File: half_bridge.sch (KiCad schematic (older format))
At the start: 9 parts, among them Q11 MOSFET_N, Q12 MOSFET_N, U6 IR2184

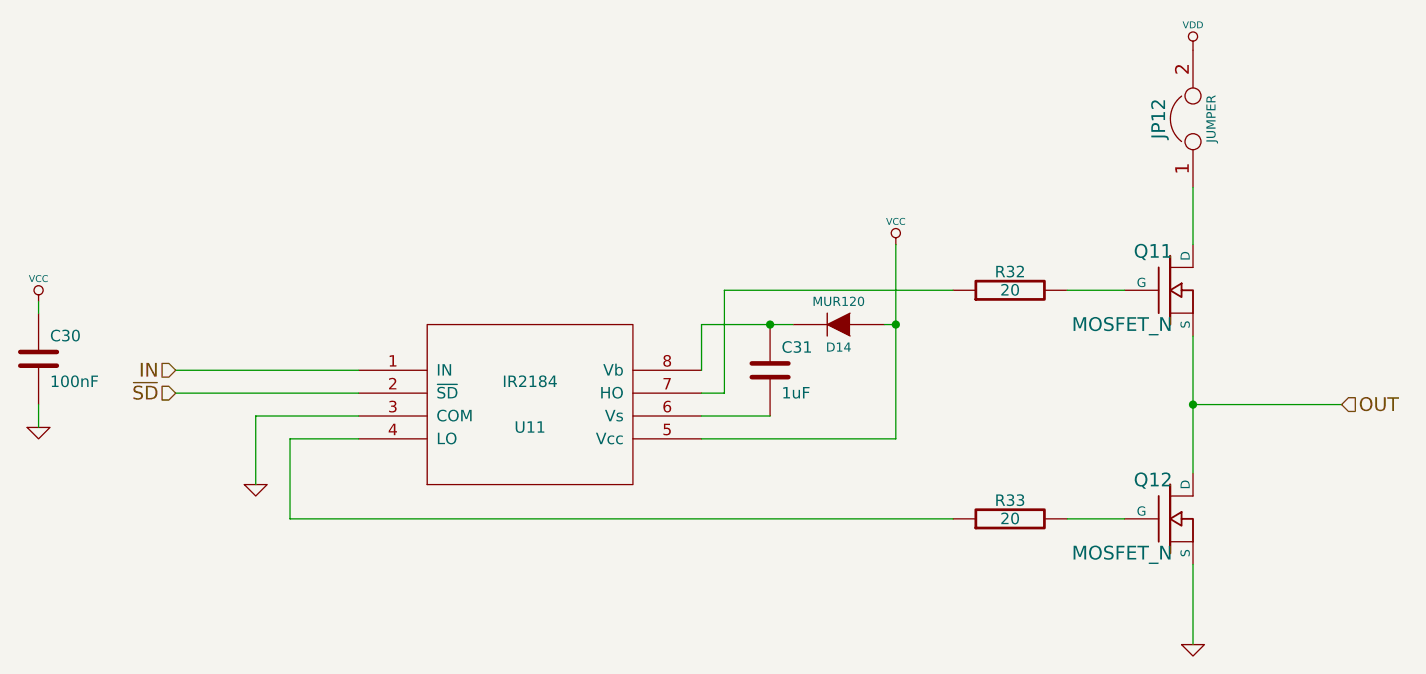
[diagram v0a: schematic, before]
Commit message: Change IR2184 to Vdd instead of Vcc
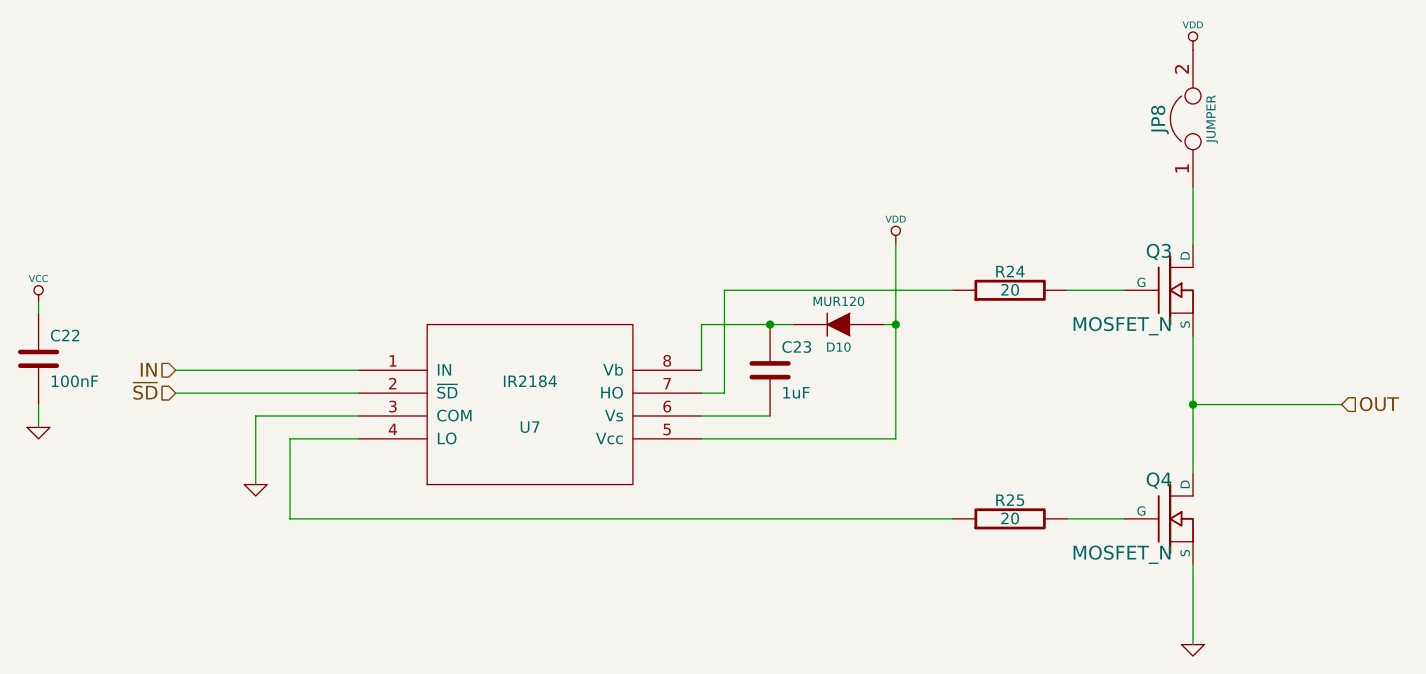
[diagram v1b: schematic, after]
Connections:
- net VCC: no longer D14.1 (A), U6.5 (Vcc)
- net VDD: now also D14.1 (A), U6.5 (Vcc)
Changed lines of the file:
@@
-EESchema Schematic File Version 2  date Fri 27 Dec 2013 06:54:03 PM EST
+EESchema Schematic File Version 2  date Sat 28 Dec 2013 06:57:52 PM EST
 LIBS:power
 LIBS:device
@@
 $Descr A4 11700 8267
 encoding utf-8
-Sheet 7 7
+Sheet 3 7
 Title "noname.sch"
-Date "27 dec 2013"
+Date "28 dec 2013"
 Rev ""
 Comp ""
@@
 Comment4 ""
 $EndDescr
+$Comp
+L VDD #PWR?
+U 1 1 52BF650C
+P 6250 2150
+F 0 "#PWR?" H 6250 2250 30  0001 C CNN
+F 1 "VDD" H 6250 2260 30  0000 C CNN
+	1    6250 2150
+	1    0    0    -1
+$EndComp
 Wire Wire Line
 	2500 2400 2500 2450
@@
 	2500 2850 2500 2950
 $Comp
-L GND #PWR066
+L GND #PWR070
 U 1 1 527843FF
 P 2500 2950
-AR Path="/52783E14/527843FF" Ref="#PWR066"  Part="1"
-AR Path="/52783E7D/527843FF" Ref="#PWR072"  Part="1"
-AR Path="/52783E4E/527843FF" Ref="#PWR078"  Part="1"
-AR Path="/52783E34/527843FF" Ref="#PWR084"  Part="1"
-AR Path="/52783943/527843FF" Ref="#PWR090"  Part="1"
-AR Path="/5278392A/527843FF" Ref="#PWR096"  Part="1"
-F 0 "#PWR096" H 2500 2950 30  0001 C CNN
+AR Path="/52783E14/527843FF" Ref="#PWR070"  Part="1"
+AR Path="/52783E7D/527843FF" Ref="#PWR076"  Part="1"
+AR Path="/52783E4E/527843FF" Ref="#PWR082"  Part="1"
+AR Path="/52783E34/527843FF" Ref="#PWR088"  Part="1"
+AR Path="/52783943/527843FF" Ref="#PWR094"  Part="1"
+AR Path="/5278392A/527843FF" Ref="#PWR0100"  Part="1"
+F 0 "#PWR076" H 2500 2950 30  0001 C CNN
 F 1 "GND" H 2500 2880 30  0001 C CNN
 	1    2500 2950
@@
 AR Path="/52783943/527843E9" Ref="C28"  Part="1"
 AR Path="/5278392A/527843E9" Ref="C30"  Part="1"
-F 0 "C30" H 2550 2750 50  0000 L CNN
+F 0 "C22" H 2550 2750 50  0000 L CNN
 F 1 "100nF" H 2550 2550 50  0000 L CNN
 	1    2500 2650
@@
 $EndComp
 $Comp
-L VCC #PWR067
+L VCC #PWR071
 U 1 1 527843E4
 P 2500 2400
-AR Path="/52783E14/527843E4" Ref="#PWR067"  Part="1"
-AR Path="/52783E7D/527843E4" Ref="#PWR073"  Part="1"
-AR Path="/52783E4E/527843E4" Ref="#PWR079"  Part="1"
-AR Path="/52783E34/527843E4" Ref="#PWR085"  Part="1"
-AR Path="/52783943/527843E4" Ref="#PWR091"  Part="1"
-AR Path="/5278392A/527843E4" Ref="#PWR097"  Part="1"
-F 0 "#PWR097" H 2500 2500 30  0001 C CNN
+AR Path="/52783E14/527843E4" Ref="#PWR071"  Part="1"
+AR Path="/52783E7D/527843E4" Ref="#PWR077"  Part="1"
+AR Path="/52783E4E/527843E4" Ref="#PWR083"  Part="1"
+AR Path="/52783E34/527843E4" Ref="#PWR089"  Part="1"
+AR Path="/52783943/527843E4" Ref="#PWR095"  Part="1"
+AR Path="/5278392A/527843E4" Ref="#PWR0101"  Part="1"
+F 0 "#PWR077" H 2500 2500 30  0001 C CNN
 F 1 "VCC" H 2500 2500 30  0000 C CNN
 	1    2500 2400
@@
 AR Path="/52783E34/527838B2" Ref="R29"  Part="1"
 AR Path="/52783943/527838B2" Ref="R31"  Part="1"
-F 0 "R33" V 6830 3350 50  0000 C CNN
+F 0 "R25" V 6830 3350 50  0000 C CNN
 F 1 "20" V 6750 3350 50  0000 C CNN
 	1    6750 3350
@@
 AR Path="/52783E34/5278387F" Ref="R28"  Part="1"
 AR Path="/52783943/5278387F" Ref="R30"  Part="1"
-F 0 "R32" V 6830 2350 50  0000 C CNN
+F 0 "R24" V 6830 2350 50  0000 C CNN
 F 1 "20" V 6750 2350 50  0000 C CNN
 	1    6750 2350
@@
 AR Path="/52783943/5278382D" Ref="U10"  Part="1"
 AR Path="/5278392A/5278382D" Ref="U11"  Part="1"
-F 0 "U11" H 4650 2750 50  0000 C CNN
+F 0 "U7" H 4650 2750 50  0000 C CNN
 F 1 "IR2184" H 4650 2950 50  0000 C CNN
 F 2 "MODULE" H 4650 2850 50  0001 C CNN
@@
 IN
 $Comp
-L GND #PWR098
+L GND #PWR0102
 U 1 1 52783639
 P 3450 3200
-AR Path="/5278392A/52783639" Ref="#PWR098"  Part="1"
-AR Path="/52783E14/52783639" Ref="#PWR068"  Part="1"
-AR Path="/52783E7D/52783639" Ref="#PWR074"  Part="1"
-AR Path="/52783E4E/52783639" Ref="#PWR080"  Part="1"
-AR Path="/52783E34/52783639" Ref="#PWR086"  Part="1"
-AR Path="/52783943/52783639" Ref="#PWR092"  Part="1"
-F 0 "#PWR098" H 3450 3200 30  0001 C CNN
+AR Path="/5278392A/52783639" Ref="#PWR0102"  Part="1"
+AR Path="/52783E14/52783639" Ref="#PWR072"  Part="1"
+AR Path="/52783E7D/52783639" Ref="#PWR078"  Part="1"
+AR Path="/52783E4E/52783639" Ref="#PWR084"  Part="1"
+AR Path="/52783E34/52783639" Ref="#PWR090"  Part="1"
+AR Path="/52783943/52783639" Ref="#PWR096"  Part="1"
+F 0 "#PWR078" H 3450 3200 30  0001 C CNN
 F 1 "GND" H 3450 3130 30  0001 C CNN
 	1    3450 3200
-	1    0    0    -1
-$EndComp
-$Comp
-L VCC #PWR099
-U 1 1 527835CC
-P 6250 2150
-AR Path="/5278392A/527835CC" Ref="#PWR099"  Part="1"
-AR Path="/52783E14/527835CC" Ref="#PWR069"  Part="1"
-AR Path="/52783E7D/527835CC" Ref="#PWR075"  Part="1"
-AR Path="/52783E4E/527835CC" Ref="#PWR081"  Part="1"
-AR Path="/52783E34/527835CC" Ref="#PWR087"  Part="1"
-AR Path="/52783943/527835CC" Ref="#PWR093"  Part="1"
-F 0 "#PWR099" H 6250 2250 30  0001 C CNN
-F 1 "VCC" H 6250 2250 30  0000 C CNN
-	1    6250 2150
 	1    0    0    -1
 $EndComp
@@
 AR Path="/52783E34/527835B9" Ref="C27"  Part="1"
 AR Path="/52783943/527835B9" Ref="C29"  Part="1"
-F 0 "C31" H 5750 2800 50  0000 L CNN
+F 0 "C23" H 5750 2800 50  0000 L CNN
 F 1 "1uF" H 5750 2600 50  0000 L CNN
 	1    5700 2700
@@
 AR Path="/52783E34/5278358E" Ref="D12"  Part="1"
 AR Path="/52783943/5278358E" Ref="D13"  Part="1"
-F 0 "D14" H 6000 2600 40  0000 C CNN
+F 0 "D10" H 6000 2600 40  0000 C CNN
 F 1 "MUR120" H 6000 2400 40  0000 C CNN
 	1    6000 2500
@@
 AR Path="/52783E34/52783118" Ref="JP10"  Part="1"
 AR Path="/52783943/52783118" Ref="JP11"  Part="1"
-F 0 "JP12" H 7550 1750 60  0000 C CNN
+F 0 "JP8" H 7550 1750 60  0000 C CNN
 F 1 "JUMPER" H 7550 1520 40  0000 C CNN
 	1    7550 1600
@@
 $EndComp
 $Comp
-L GND #PWR0100
+L GND #PWR0104
 U 1 1 52783104
 P 7550 3900
-AR Path="/5278392A/52783104" Ref="#PWR0100"  Part="1"
-AR Path="/52783E14/52783104" Ref="#PWR070"  Part="1"
-AR Path="/52783E7D/52783104" Ref="#PWR076"  Part="1"
-AR Path="/52783E4E/52783104" Ref="#PWR082"  Part="1"
-AR Path="/52783E34/52783104" Ref="#PWR088"  Part="1"
-AR Path="/52783943/52783104" Ref="#PWR094"  Part="1"
-F 0 "#PWR0100" H 7550 3900 30  0001 C CNN
+AR Path="/5278392A/52783104" Ref="#PWR0104"  Part="1"
+AR Path="/52783E14/52783104" Ref="#PWR074"  Part="1"
+AR Path="/52783E7D/52783104" Ref="#PWR080"  Part="1"
+AR Path="/52783E4E/52783104" Ref="#PWR086"  Part="1"
+AR Path="/52783E34/52783104" Ref="#PWR092"  Part="1"
+AR Path="/52783943/52783104" Ref="#PWR098"  Part="1"
+F 0 "#PWR080" H 7550 3900 30  0001 C CNN
 F 1 "GND" H 7550 3830 30  0001 C CNN
 	1    7550 3900
@@
 $EndComp
 $Comp
-L VDD #PWR0101
+L VDD #PWR0105
 U 1 1 527830FD
 P 7550 1300
-AR Path="/5278392A/527830FD" Ref="#PWR0101"  Part="1"
-AR Path="/52783E14/527830FD" Ref="#PWR071"  Part="1"
-AR Path="/52783E7D/527830FD" Ref="#PWR077"  Part="1"
-AR Path="/52783E4E/527830FD" Ref="#PWR083"  Part="1"
-AR Path="/52783E34/527830FD" Ref="#PWR089"  Part="1"
-AR Path="/52783943/527830FD" Ref="#PWR095"  Part="1"
-F 0 "#PWR0101" H 7550 1400 30  0001 C CNN
+AR Path="/5278392A/527830FD" Ref="#PWR0105"  Part="1"
+AR Path="/52783E14/527830FD" Ref="#PWR075"  Part="1"
+AR Path="/52783E7D/527830FD" Ref="#PWR081"  Part="1"
+AR Path="/52783E4E/527830FD" Ref="#PWR087"  Part="1"
+AR Path="/52783E34/527830FD" Ref="#PWR093"  Part="1"
+AR Path="/52783943/527830FD" Ref="#PWR099"  Part="1"
+F 0 "#PWR081" H 7550 1400 30  0001 C CNN
 F 1 "VDD" H 7550 1410 30  0000 C CNN
 	1    7550 1300
@@
 AR Path="/52783E34/527830EC" Ref="Q8"  Part="1"
 AR Path="/52783943/527830EC" Ref="Q10"  Part="1"
-F 0 "Q12" H 7460 3520 60  0000 R CNN
+F 0 "Q4" H 7460 3520 60  0000 R CNN
 F 1 "MOSFET_N" H 7460 3200 60  0000 R CNN
 	1    7450 3350
@@
 AR Path="/52783E34/527830DE" Ref="Q7"  Part="1"
 AR Path="/52783943/527830DE" Ref="Q9"  Part="1"
-F 0 "Q11" H 7460 2520 60  0000 R CNN
+F 0 "Q3" H 7460 2520 60  0000 R CNN
 F 1 "MOSFET_N" H 7460 2200 60  0000 R CNN
 	1    7450 2350

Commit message: Added second power connector
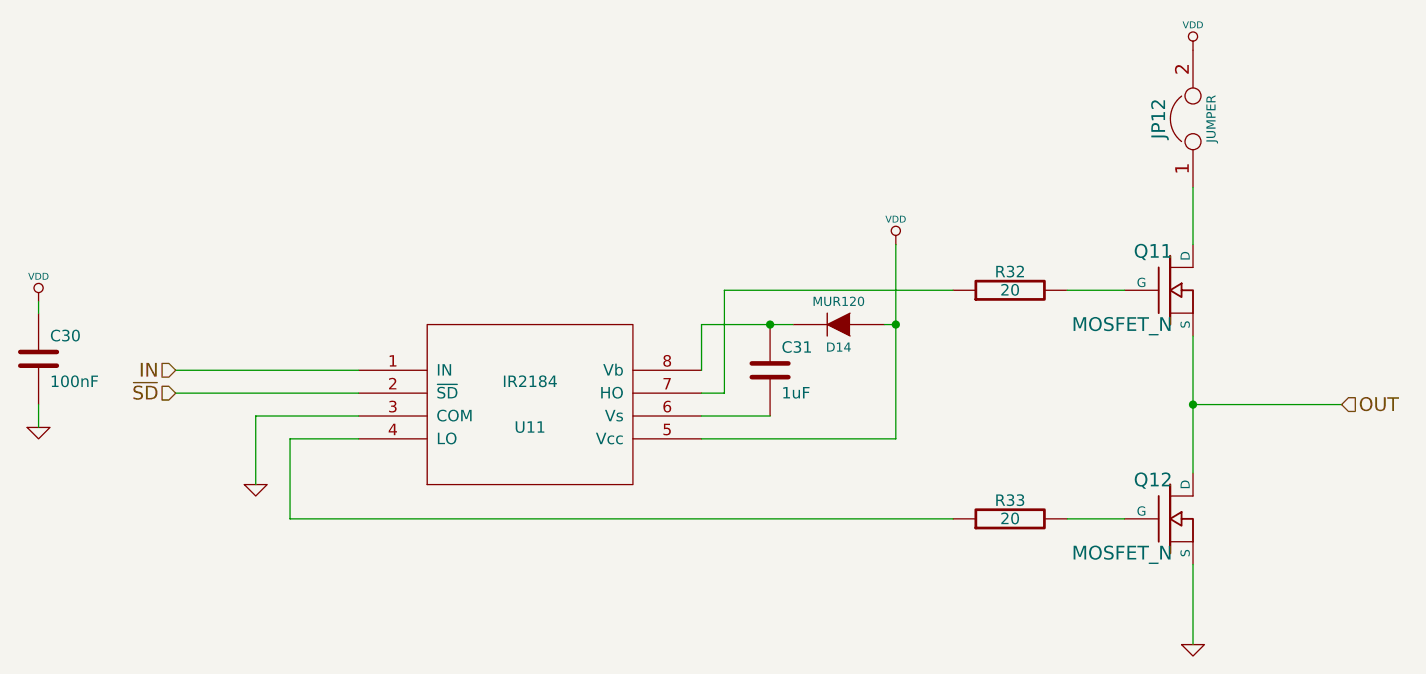
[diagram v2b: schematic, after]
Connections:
- net VCC is gone; now on net VDD: C20.1
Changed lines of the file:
@@
-EESchema Schematic File Version 2  date Sat 28 Dec 2013 06:57:52 PM EST
+EESchema Schematic File Version 2  date Thu 02 Jan 2014 06:39:32 PM EST
 LIBS:power
 LIBS:device
@@
 LIBS:-cache
 LIBS:LM25011
+LIBS:open-project
 LIBS:hackboard-cache
 EELAYER 25  0
@@
 $Descr A4 11700 8267
 encoding utf-8
-Sheet 3 7
+Sheet 4 7
 Title "noname.sch"
-Date "28 dec 2013"
+Date "2 jan 2014"
 Rev ""
 Comp ""
@@
 $EndDescr
 $Comp
-L VDD #PWR?
+L VDD #PWR70
+U 1 1 52BF660C
+P 2500 2400
+AR Path="/52783E14/52BF660C" Ref="#PWR70"  Part="1"
+AR Path="/52783E7D/52BF660C" Ref="#PWR76"  Part="1"
+AR Path="/52783E4E/52BF660C" Ref="#PWR82"  Part="1"
+AR Path="/52783E34/52BF660C" Ref="#PWR88"  Part="1"
+AR Path="/52783943/52BF660C" Ref="#PWR94"  Part="1"
+AR Path="/5278392A/52BF660C" Ref="#PWR100"  Part="1"
+F 0 "#PWR100" H 2500 2500 30  0001 C CNN
+F 1 "VDD" H 2500 2510 30  0000 C CNN
+	1    2500 2400
+	1    0    0    -1
+$EndComp
+$Comp
+L VDD #PWR79
 U 1 1 52BF650C
 P 6250 2150
-F 0 "#PWR?" H 6250 2250 30  0001 C CNN
+AR Path="/52783E7D/52BF650C" Ref="#PWR79"  Part="1"
+AR Path="/52783E14/52BF650C" Ref="#PWR73"  Part="1"
+AR Path="/52783E4E/52BF650C" Ref="#PWR85"  Part="1"
+AR Path="/52783E34/52BF650C" Ref="#PWR91"  Part="1"
+AR Path="/52783943/52BF650C" Ref="#PWR97"  Part="1"
+AR Path="/5278392A/52BF650C" Ref="#PWR103"  Part="1"
+F 0 "#PWR103" H 6250 2250 30  0001 C CNN
 F 1 "VDD" H 6250 2260 30  0000 C CNN
 	1    6250 2150
@@
 	2500 2850 2500 2950
 $Comp
-L GND #PWR070
+L GND #PWR71
 U 1 1 527843FF
 P 2500 2950
-AR Path="/52783E14/527843FF" Ref="#PWR070"  Part="1"
-AR Path="/52783E7D/527843FF" Ref="#PWR076"  Part="1"
-AR Path="/52783E4E/527843FF" Ref="#PWR082"  Part="1"
-AR Path="/52783E34/527843FF" Ref="#PWR088"  Part="1"
-AR Path="/52783943/527843FF" Ref="#PWR094"  Part="1"
-AR Path="/5278392A/527843FF" Ref="#PWR0100"  Part="1"
-F 0 "#PWR076" H 2500 2950 30  0001 C CNN
+AR Path="/52783E14/527843FF" Ref="#PWR71"  Part="1"
+AR Path="/52783E7D/527843FF" Ref="#PWR77"  Part="1"
+AR Path="/52783E4E/527843FF" Ref="#PWR83"  Part="1"
+AR Path="/52783E34/527843FF" Ref="#PWR89"  Part="1"
+AR Path="/52783943/527843FF" Ref="#PWR95"  Part="1"
+AR Path="/5278392A/527843FF" Ref="#PWR101"  Part="1"
+F 0 "#PWR101" H 2500 2950 30  0001 C CNN
 F 1 "GND" H 2500 2880 30  0001 C CNN
 	1    2500 2950
@@
 AR Path="/52783943/527843E9" Ref="C28"  Part="1"
 AR Path="/5278392A/527843E9" Ref="C30"  Part="1"
-F 0 "C22" H 2550 2750 50  0000 L CNN
+F 0 "C30" H 2550 2750 50  0000 L CNN
 F 1 "100nF" H 2550 2550 50  0000 L CNN
 	1    2500 2650
-	1    0    0    -1
-$EndComp
-$Comp
-L VCC #PWR071
-U 1 1 527843E4
-P 2500 2400
-AR Path="/52783E14/527843E4" Ref="#PWR071"  Part="1"
-AR Path="/52783E7D/527843E4" Ref="#PWR077"  Part="1"
-AR Path="/52783E4E/527843E4" Ref="#PWR083"  Part="1"
-AR Path="/52783E34/527843E4" Ref="#PWR089"  Part="1"
-AR Path="/52783943/527843E4" Ref="#PWR095"  Part="1"
-AR Path="/5278392A/527843E4" Ref="#PWR0101"  Part="1"
-F 0 "#PWR077" H 2500 2500 30  0001 C CNN
-F 1 "VCC" H 2500 2500 30  0000 C CNN
-	1    2500 2400
 	1    0    0    -1
 $EndComp
@@
 AR Path="/52783E34/527838B2" Ref="R29"  Part="1"
 AR Path="/52783943/527838B2" Ref="R31"  Part="1"
-F 0 "R25" V 6830 3350 50  0000 C CNN
+F 0 "R33" V 6830 3350 50  0000 C CNN
 F 1 "20" V 6750 3350 50  0000 C CNN
 	1    6750 3350
@@
 AR Path="/52783E34/5278387F" Ref="R28"  Part="1"
 AR Path="/52783943/5278387F" Ref="R30"  Part="1"
-F 0 "R24" V 6830 2350 50  0000 C CNN
+F 0 "R32" V 6830 2350 50  0000 C CNN
 F 1 "20" V 6750 2350 50  0000 C CNN
 	1    6750 2350
@@
 AR Path="/52783943/5278382D" Ref="U10"  Part="1"
 AR Path="/5278392A/5278382D" Ref="U11"  Part="1"
-F 0 "U7" H 4650 2750 50  0000 C CNN
+F 0 "U11" H 4650 2750 50  0000 C CNN
 F 1 "IR2184" H 4650 2950 50  0000 C CNN
 F 2 "MODULE" H 4650 2850 50  0001 C CNN
@@
 IN
 $Comp
-L GND #PWR0102
+L GND #PWR102
 U 1 1 52783639
 P 3450 3200
-AR Path="/5278392A/52783639" Ref="#PWR0102"  Part="1"
-AR Path="/52783E14/52783639" Ref="#PWR072"  Part="1"
-AR Path="/52783E7D/52783639" Ref="#PWR078"  Part="1"
-AR Path="/52783E4E/52783639" Ref="#PWR084"  Part="1"
-AR Path="/52783E34/52783639" Ref="#PWR090"  Part="1"
-AR Path="/52783943/52783639" Ref="#PWR096"  Part="1"
-F 0 "#PWR078" H 3450 3200 30  0001 C CNN
+AR Path="/5278392A/52783639" Ref="#PWR102"  Part="1"
+AR Path="/52783E14/52783639" Ref="#PWR72"  Part="1"
+AR Path="/52783E7D/52783639" Ref="#PWR78"  Part="1"
+AR Path="/52783E4E/52783639" Ref="#PWR84"  Part="1"
+AR Path="/52783E34/52783639" Ref="#PWR90"  Part="1"
+AR Path="/52783943/52783639" Ref="#PWR96"  Part="1"
+F 0 "#PWR102" H 3450 3200 30  0001 C CNN
 F 1 "GND" H 3450 3130 30  0001 C CNN
 	1    3450 3200
@@
 AR Path="/52783E34/527835B9" Ref="C27"  Part="1"
 AR Path="/52783943/527835B9" Ref="C29"  Part="1"
-F 0 "C23" H 5750 2800 50  0000 L CNN
+F 0 "C31" H 5750 2800 50  0000 L CNN
 F 1 "1uF" H 5750 2600 50  0000 L CNN
 	1    5700 2700
@@
 AR Path="/52783E34/5278358E" Ref="D12"  Part="1"
 AR Path="/52783943/5278358E" Ref="D13"  Part="1"
-F 0 "D10" H 6000 2600 40  0000 C CNN
+F 0 "D14" H 6000 2600 40  0000 C CNN
 F 1 "MUR120" H 6000 2400 40  0000 C CNN
 	1    6000 2500
@@
 AR Path="/52783E34/52783118" Ref="JP10"  Part="1"
 AR Path="/52783943/52783118" Ref="JP11"  Part="1"
-F 0 "JP8" H 7550 1750 60  0000 C CNN
+F 0 "JP12" H 7550 1750 60  0000 C CNN
 F 1 "JUMPER" H 7550 1520 40  0000 C CNN
 	1    7550 1600
@@
 $EndComp
 $Comp
-L GND #PWR0104
+L GND #PWR105
 U 1 1 52783104
 P 7550 3900
-AR Path="/5278392A/52783104" Ref="#PWR0104"  Part="1"
-AR Path="/52783E14/52783104" Ref="#PWR074"  Part="1"
-AR Path="/52783E7D/52783104" Ref="#PWR080"  Part="1"
-AR Path="/52783E4E/52783104" Ref="#PWR086"  Part="1"
-AR Path="/52783E34/52783104" Ref="#PWR092"  Part="1"
-AR Path="/52783943/52783104" Ref="#PWR098"  Part="1"
-F 0 "#PWR080" H 7550 3900 30  0001 C CNN
+AR Path="/5278392A/52783104" Ref="#PWR105"  Part="1"
+AR Path="/52783E14/52783104" Ref="#PWR75"  Part="1"
+AR Path="/52783E7D/52783104" Ref="#PWR81"  Part="1"
+AR Path="/52783E4E/52783104" Ref="#PWR87"  Part="1"
+AR Path="/52783E34/52783104" Ref="#PWR93"  Part="1"
+AR Path="/52783943/52783104" Ref="#PWR99"  Part="1"
+F 0 "#PWR105" H 7550 3900 30  0001 C CNN
 F 1 "GND" H 7550 3830 30  0001 C CNN
 	1    7550 3900
@@
 $EndComp
 $Comp
-L VDD #PWR0105
+L VDD #PWR104
 U 1 1 527830FD
 P 7550 1300
-AR Path="/5278392A/527830FD" Ref="#PWR0105"  Part="1"
-AR Path="/52783E14/527830FD" Ref="#PWR075"  Part="1"
-AR Path="/52783E7D/527830FD" Ref="#PWR081"  Part="1"
-AR Path="/52783E4E/527830FD" Ref="#PWR087"  Part="1"
-AR Path="/52783E34/527830FD" Ref="#PWR093"  Part="1"
-AR Path="/52783943/527830FD" Ref="#PWR099"  Part="1"
-F 0 "#PWR081" H 7550 1400 30  0001 C CNN
+AR Path="/5278392A/527830FD" Ref="#PWR104"  Part="1"
+AR Path="/52783E14/527830FD" Ref="#PWR74"  Part="1"
+AR Path="/52783E7D/527830FD" Ref="#PWR80"  Part="1"
+AR Path="/52783E4E/527830FD" Ref="#PWR86"  Part="1"
+AR Path="/52783E34/527830FD" Ref="#PWR92"  Part="1"
+AR Path="/52783943/527830FD" Ref="#PWR98"  Part="1"
+F 0 "#PWR104" H 7550 1400 30  0001 C CNN
 F 1 "VDD" H 7550 1410 30  0000 C CNN
 	1    7550 1300
@@
 AR Path="/52783E34/527830EC" Ref="Q8"  Part="1"
 AR Path="/52783943/527830EC" Ref="Q10"  Part="1"
-F 0 "Q4" H 7460 3520 60  0000 R CNN
+F 0 "Q12" H 7460 3520 60  0000 R CNN
 F 1 "MOSFET_N" H 7460 3200 60  0000 R CNN
 	1    7450 3350
@@
 AR Path="/52783E34/527830DE" Ref="Q7"  Part="1"
 AR Path="/52783943/527830DE" Ref="Q9"  Part="1"
-F 0 "Q3" H 7460 2520 60  0000 R CNN
+F 0 "Q11" H 7460 2520 60  0000 R CNN
 F 1 "MOSFET_N" H 7460 2200 60  0000 R CNN
 	1    7450 2350
